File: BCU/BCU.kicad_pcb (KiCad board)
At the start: 2 copper layers, 6 parts, among them IC1 STM32G474RET6, IC2 TJA1042T_3,118, IC3 LM317MDCYR, IC4 LTC6820HUD#PBF, J1 FTSH-105-01-F-DV-K-P-TR, Y1 NX2520SA-24.000000MHZ-B8

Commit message: Added some more components
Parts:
- added C1: 10V 10UF X5R, SamacSys_Parts:CAPC1608X90N, F.Cu at (127.0, 86.4)
- added C2: 25V 1UF X5R, SamacSys_Parts:CAPC1005X60N, F.Cu at (130.2, 86.2)
- added C3: 16V 100NF X7R, SamacSys_Parts:CAPC1005X55N, F.Cu at (133.1, 86.2)
- added C4: 50V 10PF C0G, SamacSys_Parts:CAPC1005X55N, F.Cu at (130.1, 88.5)
- added R1: 100K 1% 1/16W 0402, SamacSys_Parts:RESC1005X40N, F.Cu at (127.0, 88.6)
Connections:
- IC1 pad 61: unconnected-(IC1-Pad61) -> Net-(IC1-Pad61)

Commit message: update pcb+sch
pushed to pcb
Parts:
- added C10: 16V 100NF X7R, SamacSys_Parts:CAPC1005X55N, F.Cu at (153.9, 109.9)
- added C11: 50V 3.3nF X7R ±10% 0402, SamacSys_Parts:CAPC1005X55N, F.Cu at (151.5, 113.9)
- added C12: 16V 100NF X7R, SamacSys_Parts:CAPC1005X55N, F.Cu at (143.8, 121.3)
- added C13: 25V 1UF X5R, SamacSys_Parts:CAPC1005X60N, F.Cu at (139.5, 116.1)
- added C14: 22uF+/-20% 25V X5R 0805, SamacSys_Parts:CAPC2012X145N, F.Cu at (116.1, 135.7)
- added C15: 50V 56pF NP0 ±2% 0402, SamacSys_Parts:CAPC1005X55N, F.Cu at (128.0, 135.0)
- added C16: 22uF+/-20% 25V X5R 0805, SamacSys_Parts:CAPC2012X145N, F.Cu at (154.2, 105.5)
- added C17: 50V 3.3nF X7R ±10% 0402, SamacSys_Parts:CAPC1005X55N, F.Cu at (133.1, 132.9)
- added C18: 16V 100NF X7R, SamacSys_Parts:CAPC1005X55N, F.Cu at (130.8, 134.9)
- added C19: 16V 100NF X7R, SamacSys_Parts:CAPC1005X55N, F.Cu at (160.5, 105.4)
- added C20: 16V 100NF X7R, SamacSys_Parts:CAPC1005X55N, F.Cu at (148.1, 116.7)
- added C21: 16V 100NF X7R, SamacSys_Parts:CAPC1005X55N, F.Cu at (140.4, 123.5)
- added C22: 25V 1UF X5R, SamacSys_Parts:CAPC1005X60N, F.Cu at (134.4, 127.8)
- added C23: 16V 100NF X7R, SamacSys_Parts:CAPC1005X55N, F.Cu at (160.5, 103.5)
- added C24: 22uF+/-20% 25V X5R 0805, SamacSys_Parts:CAPC2012X145N, F.Cu at (112.1, 135.7)
- added C25: 16V 100NF X7R, SamacSys_Parts:CAPC1005X55N, F.Cu at (137.3, 127.4)
- added C26: 22uF+/-20% 25V X5R 0805, SamacSys_Parts:CAPC2012X145N, F.Cu at (120.1, 135.7)
- added C27: 16V 100NF X7R, SamacSys_Parts:CAPC1005X55N, F.Cu at (157.7, 105.1)
- added C28: 16V 100NF X7R, SamacSys_Parts:CAPC1005X55N, F.Cu at (152.1, 111.9)
- added C29: 25V 1UF X5R, SamacSys_Parts:CAPC1005X60N, F.Cu at (153.9, 108.0)
- added C30: 16V 100NF X7R, SamacSys_Parts:CAPC1005X55N, F.Cu at (139.5, 125.4)
- added C31: 16V 100NF X7R, SamacSys_Parts:CAPC1005X55N, F.Cu at (133.6, 130.6)
- added C32: 16V 100NF X7R, SamacSys_Parts:CAPC1005X55N, F.Cu at (146.3, 119.2)
- added C5: 100V 4.7uF X7S ±10% 1206, SamacSys_Parts:CAPC3216X180N, F.Cu at (149.9, 109.2)
- added C6: 100V 100nF X7R ±10% 0805, SamacSys_Parts:CAPC2012X135N, F.Cu at (131.0, 128.2)
- added C7: 16V 100NF X7R, SamacSys_Parts:CAPC1005X55N, F.Cu at (157.7, 107.1)
- added C8: 16V 100NF X7R, SamacSys_Parts:CAPC1005X55N, F.Cu at (163.0, 101.3)
- added C9: 50V 10PF C0G, SamacSys_Parts:CAPC1005X55N, F.Cu at (130.2, 132.9)
- added D1: MBR140SFT1G, SamacSys_Parts:SODFL3616X98N, F.Cu at (131.9, 125.3)
- added FB1: BLM15HD182SN1D, SamacSys_Parts:NFZ15SG152SN10B, F.Cu at (133.8, 122.3)
- added H1: MountingHole, MountingHole:MountingHole_2.2mm_M2, F.Cu at (203.2, 78.7)
- added H2: MountingHole, MountingHole:MountingHole_2.2mm_M2, F.Cu at (172.7, 78.7)
- added H3: MountingHole, MountingHole:MountingHole_2.2mm_M2, F.Cu at (172.7, 106.7)
- added H4: MountingHole, MountingHole:MountingHole_2.2mm_M2, F.Cu at (202.7, 106.7)
- added IC5: LM2842YQMK_NOPB, SamacSys_Parts:SOT95P280X110-6N, F.Cu at (144.0, 115.9)
- added IC6: LM5164DDAR, SamacSys_Parts:SOIC127P600X170-9N, F.Cu at (127.9, 120.4)
- added J2: SM04B-PASS-TBT_LF__SN_, SamacSys_Parts:SM04B-PASS-TBT, F.Cu at (198.1, 115.5)
- added J3: Conn_01x07_Male, Connector_PinHeader_2.54mm:PinHeader_1x07_P2.54mm_Vertical, F.Cu at (170.2, 86.4)
- added J4: SM04B-PASS-TBT_LF__SN_, SamacSys_Parts:SM04B-PASS-TBT, F.Cu at (218.4, 86.4)
- added J5: SM04B-PASS-TBT_LF__SN_, SamacSys_Parts:SM04B-PASS-TBT, F.Cu at (177.8, 116.8)
- added J6: USB_C_Receptacle_USB2.0, Connector_USB:USB_C_Receptacle_HRO_TYPE-C-31-M-12, F.Cu at (188.0, 76.2)
- added L1: CBC3225T680KRV, SamacSys_Parts:INDC3225X270N, F.Cu at (126.0, 131.9)
- added L2: SLF7045T-680MR60-PF, SamacSys_Parts:SLF7032_7045, F.Cu at (147.3, 102.9)
- added R10: 51R 1% 1/16W 0402, SamacSys_Parts:RESC1005X40N, F.Cu at (130.5, 130.9)
- added R11: 51R 1% 1/16W 0402, SamacSys_Parts:RESC1005X40N, F.Cu at (159.9, 99.3)
- added R12: 51R 1% 1/16W 0402, SamacSys_Parts:RESC1005X40N, F.Cu at (163.3, 99.3)
- added R13: 51R 1% 1/16W 0402, SamacSys_Parts:RESC1005X40N, F.Cu at (148.3, 114.7)
- added R2: 10K 1% 1/16W 0402, SamacSys_Parts:RESC1005X40N, F.Cu at (137.2, 122.1)
- added R3: 1.5K 1% 1/16W 0402, SamacSys_Parts:RESC1005X40N, F.Cu at (139.8, 119.3)
- added R4: 100K 1% 1/16W 0402, SamacSys_Parts:RESC1005X40N, F.Cu at (136.4, 124.6)
- added R5: 8.2K 1% 1/16W 0402, SamacSys_Parts:RESC1005X40N, F.Cu at (149.0, 111.9)
- added R6: 8.2K 1% 1/16W 0402, SamacSys_Parts:RESC1005X40N, F.Cu at (140.6, 121.4)
- added R7: 453kΩ 1% 402, SamacSys_Parts:RESC1005X40N, F.Cu at (143.2, 119.3)
- added R8: 453kΩ 1% 402, SamacSys_Parts:RESC1005X40N, F.Cu at (124.8, 135.1)
- added R9: 49.9K 1% 1/16W 0402, SamacSys_Parts:RESC1005X40N, F.Cu at (159.9, 101.4)
- added S1: TS-1101-C-W, SamacSys_Parts:TS1101CW, F.Cu at (188.0, 124.5)
- added S2: TS-1101-C-W, SamacSys_Parts:TS1101CW, F.Cu at (200.7, 127.0)
- added S3: TS-1101-C-W, SamacSys_Parts:TS1101CW, F.Cu at (179.2, 134.6)
- added S4: TS-1101-C-W, SamacSys_Parts:TS1101CW, F.Cu at (188.0, 132.1)
- added S5: TS-1101-C-W, SamacSys_Parts:TS1101CW, F.Cu at (175.3, 127.0)
- added T1: PE-68386NLT, SamacSys_Parts:PE68386NLT, F.Cu at (135.5, 110.0)
- J1: value FTSH-105-01-F-DV-K-P-TR -> JTAG Connector
- moved Y1 89.9 mm to (187.1, 121.3)
- moved IC1 86.6 mm to (188.0, 111.2), turned to 90 degrees
- moved IC4 82.8 mm to (190.5, 99.1), turned to 90 degrees
- moved IC3 82.0 mm to (200.0, 99.2), turned to 90 degrees
- moved R1 73.2 mm to (200.1, 90.9), turned to 90 degrees
- moved C1 71.0 mm to (197.9, 90.9), turned to 90 degrees
- moved C4 69.9 mm to (200.0, 87.8), turned to 90 degrees
- moved C2 67.5 mm to (197.7, 87.7), turned to 90 degrees
- moved C3 64.7 mm to (197.7, 84.8), turned to 90 degrees
- moved J1 64.2 mm to (179.8, 99.1), turned to 90 degrees
- moved IC2 62.1 mm to (188.8, 89.9), turned to 90 degrees
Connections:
- C1 pad 1: unconnected-(C1-Pad1) -> GND
- C1 pad 2: unconnected-(C1-Pad2) -> +3V3
- C2 pad 1: unconnected-(C2-Pad1) -> GND
- C2 pad 2: unconnected-(C2-Pad2) -> +3V3
- C3 pad 1: unconnected-(C3-Pad1) -> GND
- C3 pad 2: unconnected-(C3-Pad2) -> +5V
- C4 pad 1: unconnected-(C4-Pad1) -> GND
- C4 pad 2: unconnected-(C4-Pad2) -> Net-(Y1-Pad3)
- IC1 pad 1: unconnected-(IC1-Pad1) -> +3V3
- IC1 pad 10: unconnected-(IC1-Pad10) -> /BTN_LEFT
- IC1 pad 11: unconnected-(IC1-Pad11) -> /BTN_RIGHT
- IC1 pad 12: unconnected-(IC1-Pad12) -> /BTN_PWR
- IC1 pad 13: unconnected-(IC1-Pad13) -> /ADC_BRAKE
- IC1 pad 14: unconnected-(IC1-Pad14) -> /ADC_THROT
- IC1 pad 15: unconnected-(IC1-Pad15) -> GND
- IC1 pad 16: unconnected-(IC1-Pad16) -> +3V3
- IC1 pad 17: unconnected-(IC1-Pad17) -> /ADC_TORQUE
- IC1 pad 18: unconnected-(IC1-Pad18) -> /OLED_CS
- IC1 pad 19: unconnected-(IC1-Pad19) -> /OLED_CLK
- IC1 pad 21: unconnected-(IC1-Pad21) -> /OLED_DIN
- IC1 pad 22: unconnected-(IC1-Pad22) -> /OLED_RST
- IC1 pad 27: unconnected-(IC1-Pad27) -> +3.3VA
- IC1 pad 28: unconnected-(IC1-Pad28) -> GND
- IC1 pad 29: unconnected-(IC1-Pad29) -> +3.3VA
- IC1 pad 30: unconnected-(IC1-Pad30) -> /OLED_DC
- IC1 pad 31: unconnected-(IC1-Pad31) -> GND
- IC1 pad 32: unconnected-(IC1-Pad32) -> +3V3
- IC1 pad 34: unconnected-(IC1-Pad34) -> Net-(IC1-Pad34)
- IC1 pad 35: unconnected-(IC1-Pad35) -> Net-(IC1-Pad35)
- IC1 pad 36: unconnected-(IC1-Pad36) -> Net-(IC1-Pad36)
- IC1 pad 37: unconnected-(IC1-Pad37) -> Net-(IC1-Pad37)
- IC1 pad 47: unconnected-(IC1-Pad47) -> GND
- IC1 pad 48: unconnected-(IC1-Pad48) -> +3V3
- IC1 pad 49: unconnected-(IC1-Pad49) -> /JTAG_TMS
- IC1 pad 5: unconnected-(IC1-Pad5) -> Net-(Y1-Pad1)
- IC1 pad 50: unconnected-(IC1-Pad50) -> /JTAG_TCK
- IC1 pad 51: unconnected-(IC1-Pad51) -> /JTAG_TDI
- IC1 pad 56: unconnected-(IC1-Pad56) -> /JTAG_TDO
- IC1 pad 59: unconnected-(IC1-Pad59) -> Net-(IC2-Pad1)
- IC1 pad 6: unconnected-(IC1-Pad6) -> Net-(Y1-Pad3)
- IC1 pad 60: unconnected-(IC1-Pad60) -> Net-(IC2-Pad4)
- IC1 pad 63: unconnected-(IC1-Pad63) -> GND
- IC1 pad 64: unconnected-(IC1-Pad64) -> +3V3
- IC1 pad 7: unconnected-(IC1-Pad7) -> /nRESET
- IC1 pad 8: unconnected-(IC1-Pad8) -> /BTN_UP
- IC1 pad 9: unconnected-(IC1-Pad9) -> /BTN_DOWN
- IC2 pad 1: unconnected-(IC2-Pad1) -> Net-(IC2-Pad1)
- IC2 pad 2: unconnected-(IC2-Pad2) -> GND
- IC2 pad 3: unconnected-(IC2-Pad3) -> +5V
- IC2 pad 4: unconnected-(IC2-Pad4) -> Net-(IC2-Pad4)
- IC2 pad 5: unconnected-(IC2-Pad5) -> +3V3
- IC2 pad 6: unconnected-(IC2-Pad6) -> Net-(IC2-Pad6)
- IC2 pad 7: unconnected-(IC2-Pad7) -> Net-(IC2-Pad7)
- IC2 pad 8: unconnected-(IC2-Pad8) -> GND
- IC3 pad 1: unconnected-(IC3-Pad1) -> Net-(IC3-Pad1)
- IC3 pad 2: unconnected-(IC3-Pad2) -> +3V3
- IC3 pad 3: unconnected-(IC3-Pad3) -> +5V
- IC3 pad 4: unconnected-(IC3-Pad4) -> +3V3
- IC4 pad 1: unconnected-(IC4-Pad1) -> Net-(IC1-Pad37)
- IC4 pad 10: unconnected-(IC4-Pad10) -> Net-(IC4-Pad10)
- IC4 pad 2: unconnected-(IC4-Pad2) -> Net-(IC1-Pad36)
- IC4 pad 3: unconnected-(IC4-Pad3) -> Net-(IC1-Pad35)
- IC4 pad 4: unconnected-(IC4-Pad4) -> Net-(IC1-Pad34)
- IC4 pad 9: unconnected-(IC4-Pad9) -> Net-(IC4-Pad9)
- J1 pad 1: unconnected-(J1-Pad1) -> +3V3
- J1 pad 10: unconnected-(J1-Pad10) -> /nRESET
- J1 pad 2: unconnected-(J1-Pad2) -> /JTAG_TMS
- J1 pad 3: unconnected-(J1-Pad3) -> GND
- J1 pad 4: unconnected-(J1-Pad4) -> /JTAG_TCK
- J1 pad 5: unconnected-(J1-Pad5) -> GND
- J1 pad 6: unconnected-(J1-Pad6) -> /JTAG_TDO
- J1 pad 8: unconnected-(J1-Pad8) -> /JTAG_TDI
- J1 pad 9: unconnected-(J1-Pad9) -> GND
- Y1 pad 1: unconnected-(Y1-Pad1) -> Net-(Y1-Pad1)
- Y1 pad 2: unconnected-(Y1-Pad2) -> GND
- Y1 pad 3: unconnected-(Y1-Pad3) -> Net-(Y1-Pad3)
- Y1 pad 4: unconnected-(Y1-Pad4) -> GND

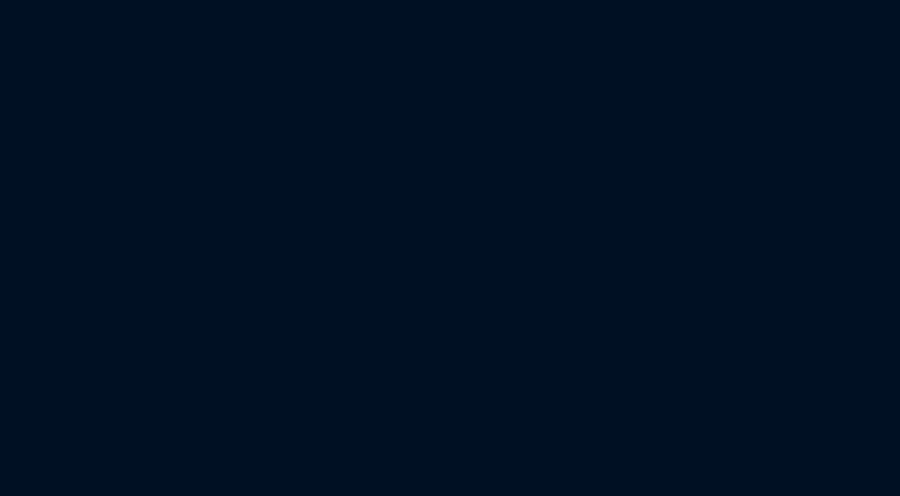
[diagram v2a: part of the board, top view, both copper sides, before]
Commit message: Migrate schemtaic to coilchain library
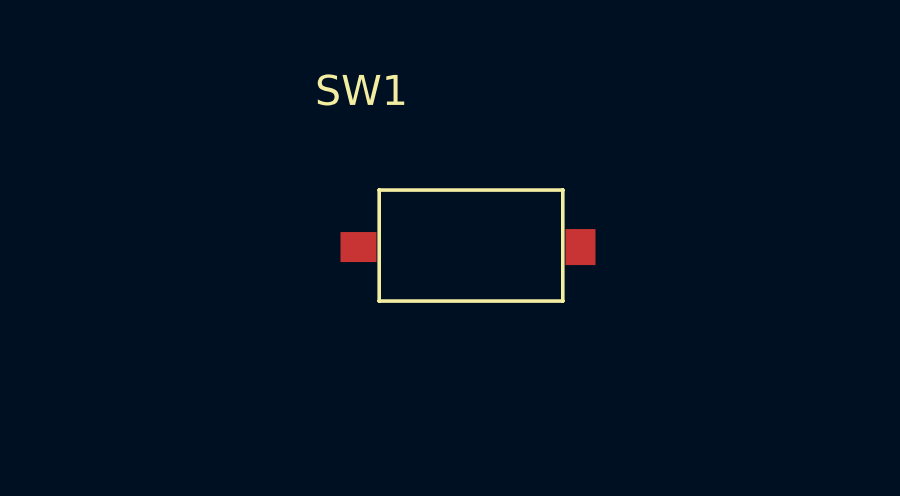
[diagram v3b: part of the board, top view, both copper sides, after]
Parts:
- added SW1: SW_Push, coilchain-switch:TS-1101-C-W, F.Cu at (152.5, 71.0)
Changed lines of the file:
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@@
   (net 40 "+3V3")
   (net 41 "+5V")
-  (net 42 "Net-(Y1-Pad3)")
+  (net 42 "Net-(C4-Pad2)")
   (net 43 "Net-(C5-Pad2)")
   (net 44 "+12V")
   (net 45 "Net-(C8-Pad1)")
   (net 46 "Net-(C8-Pad2)")
-  (net 47 "Net-(Y1-Pad1)")
+  (net 47 "Net-(C9-Pad2)")
   (net 48 "Net-(C11-Pad1)")
   (net 49 "Net-(C11-Pad2)")
@@
   (net 75 "/JTAG_TDI")
   (net 76 "/JTAG_TDO")
-  (net 77 "Net-(IC2-Pad1)")
-  (net 78 "Net-(IC2-Pad4)")
+  (net 77 "Net-(IC1-Pad59)")
+  (net 78 "Net-(IC1-Pad60)")
   (net 79 "Net-(IC2-Pad6)")
   (net 80 "Net-(IC2-Pad7)")
@@
   (net 115 "unconnected-(S5-Pad1)")
   (net 116 "unconnected-(S5-Pad2)")
+  (net 117 "unconnected-(SW1-Pad1)")
+  (net 118 "unconnected-(SW1-Pad2)")
   (footprint "SamacSys_Parts:SM04B-PASS-TBT" (layer "F.Cu")
     (at 198.12 115.46 -90)
@@
       (net 3 "unconnected-(IC1-Pad4)") (pinfunction "PC15-OSC32_OUT") (pintype "passive"))
     (pad "5" smd rect locked (at -5.738 -1.75 180) (size 0.3 1.475) (layers "F.Cu" "F.Paste" "F.Mask")
-      (net 47 "Net-(Y1-Pad1)") (pinfunction "PF0-OSC_IN") (pintype "passive"))
+      (net 47 "Net-(C9-Pad2)") (pinfunction "PF0-OSC_IN") (pintype "passive"))
     (pad "6" smd rect locked (at -5.738 -1.25 180) (size 0.3 1.475) (layers "F.Cu" "F.Paste" "F.Mask")
-      (net 42 "Net-(Y1-Pad3)") (pinfunction "PF1-OSC_OUT") (pintype "passive"))
+      (net 42 "Net-(C4-Pad2)") (pinfunction "PF1-OSC_OUT") (pintype "passive"))
     (pad "7" smd rect locked (at -5.738 -0.75 180) (size 0.3 1.475) (layers "F.Cu" "F.Paste" "F.Mask")
       (net 55 "/nRESET") (pinfunction "PG10-NRST") (pintype "passive"))
@@
       (net 24 "unconnected-(IC1-Pad58)") (pinfunction "PB5") (pintype "passive"))
     (pad "59" smd rect locked (at -1.25 -5.738 90) (size 0.3 1.475) (layers "F.Cu" "F.Paste" "F.Mask")
-      (net 77 "Net-(IC2-Pad1)") (pinfunction "PB6") (pintype "passive"))
+      (net 77 "Net-(IC1-Pad59)") (pinfunction "PB6") (pintype "passive"))
     (pad "60" smd rect locked (at -1.75 -5.738 90) (size 0.3 1.475) (layers "F.Cu" "F.Paste" "F.Mask")
-      (net 78 "Net-(IC2-Pad4)") (pinfunction "PB7") (pintype "passive"))
+      (net 78 "Net-(IC1-Pad60)") (pinfunction "PB7") (pintype "passive"))
     (pad "61" smd rect locked (at -2.25 -5.738 90) (size 0.3 1.475) (layers "F.Cu" "F.Paste" "F.Mask")
       (net 38 "Net-(IC1-Pad61)") (pinfunction "PB8-BOOT0") (pintype "passive"))
@@
       (net 39 "GND") (pintype "passive"))
     (pad "2" smd rect locked (at 0.46 0) (size 0.6 0.62) (layers "F.Cu" "F.Paste" "F.Mask")
-      (net 47 "Net-(Y1-Pad1)") (pintype "passive"))
+      (net 47 "Net-(C9-Pad2)") (pintype "passive"))
     (model "C:\\Users\\jtuma\\OneDrive\\Documents\\KiCad\\SamacSys\\SamacSys_Parts.3dshapes\\CC0402GRNPO9BN560.stp"
       (offset (xyz 0 0 0))
@@
       (net 39 "GND") (pintype "passive"))
     (pad "2" smd rect locked (at 0.46 0 90) (size 0.6 0.62) (layers "F.Cu" "F.Paste" "F.Mask")
-      (net 42 "Net-(Y1-Pad3)") (pintype "passive"))
+      (net 42 "Net-(C4-Pad2)") (pintype "passive"))
     (model "C:\\Users\\jtuma\\OneDrive\\Documents\\KiCad\\SamacSys\\SamacSys_Parts.3dshapes\\CC0402GRNPO9BN560.stp"
       (offset (xyz 0 0 0))
@@
     (fp_line (start 1.25 -1) (end -1.25 -1) (layer "F.Fab") (width 0.1))
     (pad "1" smd rect locked (at -0.85 0.65 90) (size 1 1.2) (layers "F.Cu" "F.Paste" "F.Mask")
-      (net 47 "Net-(Y1-Pad1)") (pinfunction "X1") (pintype "passive"))
+      (net 47 "Net-(C9-Pad2)") (pinfunction "X1") (pintype "passive"))
     (pad "2" smd rect locked (at 0.85 0.65 90) (size 1 1.2) (layers "F.Cu" "F.Paste" "F.Mask")
       (net 39 "GND") (pinfunction "GND_1") (pintype "passive"))
     (pad "3" smd rect locked (at 0.85 -0.65 90) (size 1 1.2) (layers "F.Cu" "F.Paste" "F.Mask")
-      (net 42 "Net-(Y1-Pad3)") (pinfunction "X2") (pintype "passive"))
+      (net 42 "Net-(C4-Pad2)") (pinfunction "X2") (pintype "passive"))
     (pad "4" smd rect locked (at -0.85 -0.65 90) (size 1 1.2) (layers "F.Cu" "F.Paste" "F.Mask")
       (net 39 "GND") (pinfunction "GND_2") (pintype "passive"))
@@
     (fp_line (start -1.95 -2.45) (end 1.95 -2.45) (layer "F.Fab") (width 0.1))
     (pad "1" smd rect locked (at -2.725 -1.905 180) (size 0.7 1.55) (layers "F.Cu" "F.Paste" "F.Mask")
-      (net 77 "Net-(IC2-Pad1)") (pinfunction "TXD") (pintype "passive"))
+      (net 77 "Net-(IC1-Pad59)") (pinfunction "TXD") (pintype "passive"))
     (pad "2" smd rect locked (at -2.725 -0.635 180) (size 0.7 1.55) (layers "F.Cu" "F.Paste" "F.Mask")
       (net 39 "GND") (pinfunction "GND") (pintype "passive"))
@@
       (net 41 "+5V") (pinfunction "VCC") (pintype "passive"))
     (pad "4" smd rect locked (at -2.725 1.905 180) (size 0.7 1.55) (layers "F.Cu" "F.Paste" "F.Mask")
-      (net 78 "Net-(IC2-Pad4)") (pinfunction "RXD") (pintype "passive"))
+      (net 78 "Net-(IC1-Pad60)") (pinfunction "RXD") (pintype "passive"))
     (pad "5" smd rect locked (at 2.725 1.905 180) (size 0.7 1.55) (layers "F.Cu" "F.Paste" "F.Mask")
       (net 40 "+3V3") (pinfunction "VIO") (pintype "passive"))
@@
     )
   )
+  (footprint "coilchain-switch:TS-1101-C-W" (layer "F.Cu")
+    (at 152.5 71)
+    (property "Sheetfile" "BCU.kicad_sch")
+    (property "Sheetname" "")
+    (attr smd)
+    (fp_text reference "SW1" (at -3.6 -5.2 unlocked) (layer "F.SilkS")
+      (effects (font (size 1 1) (thickness 0.15)))
+    )
+    (fp_text value "SW_Push" (at 0 -3.4 unlocked) (layer "F.Fab")
+      (effects (font (size 1 1) (thickness 0.15)))
+    )
+    (fp_line (start 3.11 1.8) (end -3.01 1.8) (layer "F.SilkS") (width 0.12))
+    (fp_line (start 3.11 -1.9) (end 3.11 1.8) (layer "F.SilkS") (width 0.12))
+    (fp_line (start -3.01 -1.9) (end 3.11 -1.9) (layer "F.SilkS") (width 0.12))
+    (fp_line (start -3.01 1.8) (end -3.01 -1.9) (layer "F.SilkS") (width 0.12))
+    (fp_line (start 4.3 2) (end -4.4 2) (layer "F.CrtYd") (width 0.05))
+    (fp_line (start 4.3 -2.1) (end 4.3 2) (layer "F.CrtYd") (width 0.05))
+    (fp_line (start -4.4 2) (end -4.4 -2.1) (layer "F.CrtYd") (width 0.05))
+    (fp_line (start -4.4 -2.1) (end 4.3 -2.1) (layer "F.CrtYd") (width 0.05))
+    (fp_line (start 3.05 -1.85) (end 3.05 1.75) (layer "F.Fab") (width 0.1))
+    (fp_line (start -2.95 1.75) (end 3.05 1.75) (layer "F.Fab") (width 0.1))
+    (fp_line (start -1.45 -0.85) (end 1.55 -0.85) (layer "F.Fab") (width 0.1))
+    (fp_line (start -1.45 0.75) (end 1.55 0.75) (layer "F.Fab") (width 0.1))
+    (fp_line (start -1.7 0.95) (end -1.7 -1.05) (layer "F.Fab") (width 0.1))
+    (fp_line (start -2.95 -1.85) (end 3.05 -1.85) (layer "F.Fab") (width 0.1))
+    (fp_line (start 1.55 -0.85) (end 1.55 0.75) (layer "F.Fab") (width 0.1))
+    (fp_line (start -1.45 -0.85) (end -1.45 0.75) (layer "F.Fab") (width 0.1))
+    (fp_line (start -2.95 -1.85) (end -2.95 1.75) (layer "F.Fab") (width 0.1))
+    (fp_line (start 1.8 0.95) (end -1.7 0.95) (layer "F.Fab") (width 0.1))
+    (fp_line (start 1.8 -1.05) (end 1.8 0.95) (layer "F.Fab") (width 0.1))
+    (fp_line (start -1.7 -1.05) (end 1.8 -1.05) (layer "F.Fab") (width 0.1))
+    (pad "1" smd rect (at -3.7 0) (size 1.2 1) (layers "F.Cu" "F.Paste" "F.Mask")
+      (net 117 "unconnected-(SW1-Pad1)") (pinfunction "1") (pintype "passive"))
+    (pad "2" smd rect (at 3.7 0) (size 1 1.2) (layers "F.Cu" "F.Paste" "F.Mask")
+      (net 118 "unconnected-(SW1-Pad2)") (pinfunction "2") (pintype "passive"))
+    (model "COILCHAIN3D:/coilchain-switch/TS-1101-X-X.stp"
+      (offset (xyz 0 0 0))
+      (scale (xyz 1 1 1))
+      (rotate (xyz -90 0 0))
+    )
+  )
